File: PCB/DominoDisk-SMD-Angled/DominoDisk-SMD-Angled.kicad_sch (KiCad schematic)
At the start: 28 parts, among them J1 Daisy port out, J2 ICSP_ISP6, J3 UART, J4 Daisy port in, K1 HYC77-TF09-200, U1 PC817C-S, U2 ATmega328P-AU, U3 SE5218, U4 TXB0104QPWRQ1, Y1 Crystal_GND2

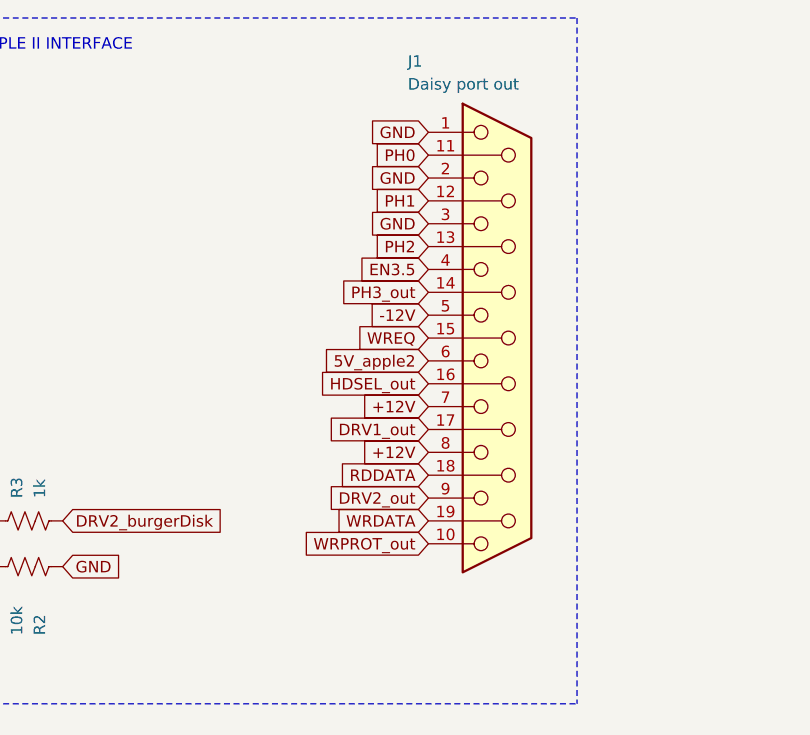
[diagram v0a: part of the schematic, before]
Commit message: Cleanup PCBs, fatter power traces
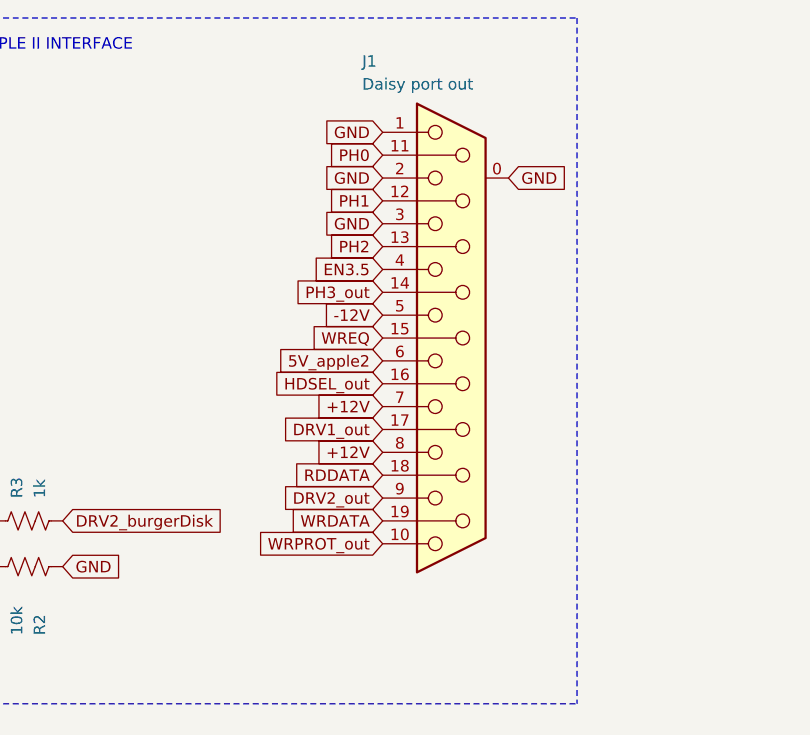
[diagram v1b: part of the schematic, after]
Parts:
- J1: footprint db19:DSUB-19_Female_EdgeMount_Pitch2.77mm -> DSUB-19-angled:DSUB-19_Female_Horizontal_MXS82009-8251-9246
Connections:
- net GND: now also J1.0 (GND)

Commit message: Add libraries and update Domino/Angled
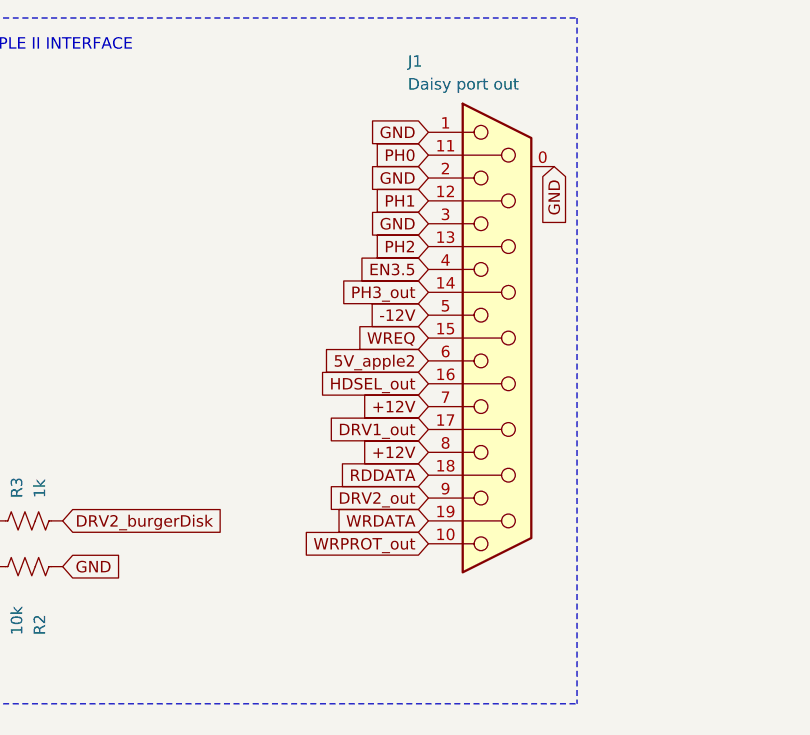
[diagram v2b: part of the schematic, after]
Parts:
- C2: value 100nF -> 100n; LCSC C28233 -> C1590
- K1: footprint MICROSD-HYC77-TF09-200:MICROSD-HYC77-TF09-200 -> HYC04-TF09-200:MICROSD-HYC77-TF09-200
- R4: value 10K -> 10k; LCSC C17414 -> C177337
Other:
- moved on the sheet: J1
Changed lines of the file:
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@@
 	(global_label "+12V"
 		(shape input)
-		(at 140.97 63.5 180)
+		(at 146.05 63.5 180)
 		(fields_autoplaced yes)
 		(effects
@@
 		)
 		(property "Intersheetrefs" "${INTERSHEET_REFS}"
-			(at 132.9048 63.5 0)
+			(at 137.9848 63.5 0)
 			(effects
 				(font
@@
 	(global_label "WRDATA"
 		(shape input)
-		(at 140.97 71.12 180)
+		(at 146.05 71.12 180)
 		(fields_autoplaced yes)
 		(effects
@@
 		)
 		(property "Intersheetrefs" "${INTERSHEET_REFS}"
-			(at 130.8486 71.12 0)
+			(at 135.9286 71.12 0)
 			(effects
 				(font
@@
 	(global_label "-12V"
 		(shape input)
-		(at 140.97 48.26 180)
+		(at 146.05 48.26 180)
 		(fields_autoplaced yes)
 		(effects
@@
 		)
 		(property "Intersheetrefs" "${INTERSHEET_REFS}"
-			(at 132.9048 48.26 0)
+			(at 137.9848 48.26 0)
 			(effects
 				(font
@@
 	(global_label "DRV2_out"
 		(shape input)
-		(at 140.97 68.58 180)
+		(at 146.05 68.58 180)
 		(fields_autoplaced yes)
 		(effects
@@
 		)
 		(property "Intersheetrefs" "${INTERSHEET_REFS}"
-			(at 129.1554 68.58 0)
+			(at 134.2354 68.58 0)
 			(effects
 				(font
@@
 	(global_label "GND"
 		(shape input)
-		(at 140.97 38.1 180)
+		(at 146.05 38.1 180)
 		(fields_autoplaced yes)
 		(effects
@@
 		)
 		(property "Intersheetrefs" "${INTERSHEET_REFS}"
-			(at 134.1143 38.1 0)
+			(at 139.1943 38.1 0)
 			(effects
 				(font
@@
 	(global_label "HDSEL_out"
 		(shape input)
-		(at 140.97 55.88 180)
+		(at 146.05 55.88 180)
 		(fields_autoplaced yes)
 		(effects
@@
 		)
 		(property "Intersheetrefs" "${INTERSHEET_REFS}"
-			(at 128.0064 55.88 0)
+			(at 133.0864 55.88 0)
+			(effects
+				(font
+					(size 1.27 1.27)
+				)
+				(justify right)
+				(hide yes)
+			)
+		)
+	)
+	(global_label "GND"
+		(shape input)
+		(at 160.02 31.75 270)
+		(fields_autoplaced yes)
+		(effects
+			(font
+				(size 1.27 1.27)
+			)
+			(justify right)
+		)
+		(property "Intersheetrefs" "${INTERSHEET_REFS}"
+			(at 160.02 38.6057 90)
 			(effects
 				(font
@@
 	(global_label "PH0"
 		(shape input)
-		(at 140.97 30.48 180)
+		(at 146.05 30.48 180)
 		(fields_autoplaced yes)
 		(effects
@@
 		)
 		(property "Intersheetrefs" "${INTERSHEET_REFS}"
-			(at 134.1748 30.48 0)
+			(at 139.2548 30.48 0)
 			(effects
 				(font
@@
 	(global_label "GND"
 		(shape input)
-		(at 154.94 33.02 0)
-		(fields_autoplaced yes)
-		(effects
-			(font
-				(size 1.27 1.27)
-			)
-			(justify left)
-		)
-		(property "Intersheetrefs" "${INTERSHEET_REFS}"
-			(at 161.7957 33.02 0)
-			(effects
-				(font
-					(size 1.27 1.27)
-				)
-				(justify left)
-				(hide yes)
-			)
-		)
-	)
-	(global_label "GND"
-		(shape input)
 		(at 41.91 27.94 0)
 		(fields_autoplaced yes)
@@
 	(global_label "RDDATA"
 		(shape input)
-		(at 140.97 66.04 180)
+		(at 146.05 66.04 180)
 		(fields_autoplaced yes)
 		(effects
@@
 		)
 		(property "Intersheetrefs" "${INTERSHEET_REFS}"
-			(at 131.03 66.04 0)
+			(at 136.11 66.04 0)
 			(effects
 				(font
@@
 	(global_label "GND"
 		(shape input)
-		(at 140.97 27.94 180)
+		(at 146.05 27.94 180)
 		(fields_autoplaced yes)
 		(effects
@@
 		)
 		(property "Intersheetrefs" "${INTERSHEET_REFS}"
-			(at 134.1143 27.94 0)
+			(at 139.1943 27.94 0)
 			(effects
 				(font
@@
 	(global_label "5V_apple2"
 		(shape input)
-		(at 140.97 53.34 180)
+		(at 146.05 53.34 180)
 		(fields_autoplaced yes)
 		(effects
@@
 		)
 		(property "Intersheetrefs" "${INTERSHEET_REFS}"
-			(at 128.3088 53.34 0)
+			(at 133.3888 53.34 0)
 			(effects
 				(font
@@
 	(global_label "GND"
 		(shape input)
-		(at 140.97 33.02 180)
+		(at 146.05 33.02 180)
 		(fields_autoplaced yes)
 		(effects
@@
 		)
 		(property "Intersheetrefs" "${INTERSHEET_REFS}"
-			(at 134.1143 33.02 0)
+			(at 139.1943 33.02 0)
 			(effects
 				(font
@@
 	(global_label "WREQ"
 		(shape input)
-		(at 140.97 50.8 180)
+		(at 146.05 50.8 180)
 		(fields_autoplaced yes)
 		(effects
@@
 		)
 		(property "Intersheetrefs" "${INTERSHEET_REFS}"
-			(at 132.7839 50.8 0)
+			(at 137.8639 50.8 0)
 			(effects
 				(font
@@
 	(global_label "DRV1_out"
 		(shape input)
-		(at 140.97 60.96 180)
+		(at 146.05 60.96 180)
 		(fields_autoplaced yes)
 		(effects
@@
 		)
 		(property "Intersheetrefs" "${INTERSHEET_REFS}"
-			(at 129.1554 60.96 0)
+			(at 134.2354 60.96 0)
 			(effects
 				(font
@@
 	(global_label "PH2"
 		(shape input)
-		(at 140.97 40.64 180)
+		(at 146.05 40.64 180)
 		(fields_autoplaced yes)
 		(effects
@@
 		)
 		(property "Intersheetrefs" "${INTERSHEET_REFS}"
-			(at 134.1748 40.64 0)
+			(at 139.2548 40.64 0)
 			(effects
 				(font
@@
 	(global_label "PH1"
 		(shape input)
-		(at 140.97 35.56 180)
+		(at 146.05 35.56 180)
 		(fields_autoplaced yes)
 		(effects
@@
 		)
 		(property "Intersheetrefs" "${INTERSHEET_REFS}"
-			(at 134.1748 35.56 0)
+			(at 139.2548 35.56 0)
 			(effects
 				(font
@@
 	(global_label "EN3.5"
 		(shape input)
-		(at 140.97 43.18 180)
+		(at 146.05 43.18 180)
 		(fields_autoplaced yes)
 		(effects
@@
 		)
 		(property "Intersheetrefs" "${INTERSHEET_REFS}"
-			(at 132.4815 43.18 0)
+			(at 137.5615 43.18 0)
 			(effects
 				(font
@@
 	(global_label "PH3_out"
 		(shape input)
-		(at 140.97 45.72 180)
+		(at 146.05 45.72 180)
 		(fields_autoplaced yes)
 		(effects
@@
 		)
 		(property "Intersheetrefs" "${INTERSHEET_REFS}"
-			(at 130.1835 45.72 0)
+			(at 135.2635 45.72 0)
 			(effects
 				(font
@@
 	(global_label "+12V"
 		(shape input)
-		(at 140.97 58.42 180)
+		(at 146.05 58.42 180)
 		(fields_autoplaced yes)
 		(effects
@@
 		)
 		(property "Intersheetrefs" "${INTERSHEET_REFS}"
-			(at 132.9048 58.42 0)
+			(at 137.9848 58.42 0)
 			(effects
 				(font
@@
 	(global_label "WRPROT_out"
 		(shape input)
-		(at 140.97 73.66 180)
+		(at 146.05 73.66 180)
 		(fields_autoplaced yes)
 		(effects
@@
 		)
 		(property "Intersheetrefs" "${INTERSHEET_REFS}"
-			(at 126.434 73.66 0)
+			(at 131.514 73.66 0)
 			(effects
 				(font
@@
 			)
 		)
-		(property "Value" "100nF"
+		(property "Value" "100n"
 			(at 25.7048 118.11 90)
 			(effects
@@
 			)
 		)
-		(property "LCSC" "C28233"
+		(property "LCSC" " C1590"
 			(at 29.21 118.11 90)
 			(effects
@@
 	(symbol
 		(lib_id "db19:DB19_Female")
-		(at 148.59 50.8 0)
+		(at 153.67 50.8 0)
 		(unit 1)
 		(exclude_from_sim no)
@@
 		(dnp no)
 		(property "Reference" "J1"
-			(at 138.684 20.066 0)
+			(at 143.764 20.066 0)
 			(effects
 				(font
@@
 		)
 		(property "Value" "Daisy port out"
-			(at 138.684 22.606 0)
+			(at 143.764 22.606 0)
 			(effects
 				(font
@@
 		)
 		(property "Footprint" "DSUB-19-angled:DSUB-19_Female_Horizontal_MXS82009-8251-9246"
-			(at 148.59 58.42 0)
+			(at 153.67 58.42 0)
 			(effects
 				(font
@@
 		)
 		(property "Datasheet" ""
-			(at 148.59 58.42 0)
+			(at 153.67 58.42 0)
 			(effects
 				(font
@@
 		)
 		(property "Description" ""
-			(at 148.59 50.8 0)
+			(at 153.67 50.8 0)
 			(effects
 				(font
@@
 			)
 		)
-		(property "Footprint" "MICROSD-HYC77-TF09-200:MICROSD-HYC77-TF09-200"
+		(property "Footprint" "HYC04-TF09-200:MICROSD-HYC77-TF09-200"
 			(at 269.24 50.8 0)
 			(effects
@@
 			)
 		)
-		(property "Value" "10K"
+		(property "Value" "10k"
 			(at 108.4072 147.193 0)
 			(effects
@@
 			)
 		)
-		(property "LCSC" "C17414"
+		(property "LCSC" " C177337"
 			(at 106.68 146.05 0)
 			(effects

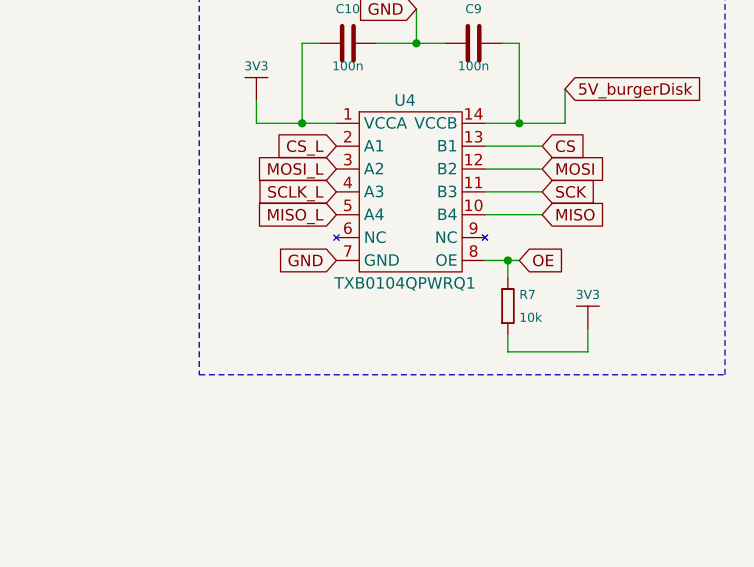
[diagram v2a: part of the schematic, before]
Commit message: Add logo (thanks to Javier Rivera!!)
Add my own micro/SD modules
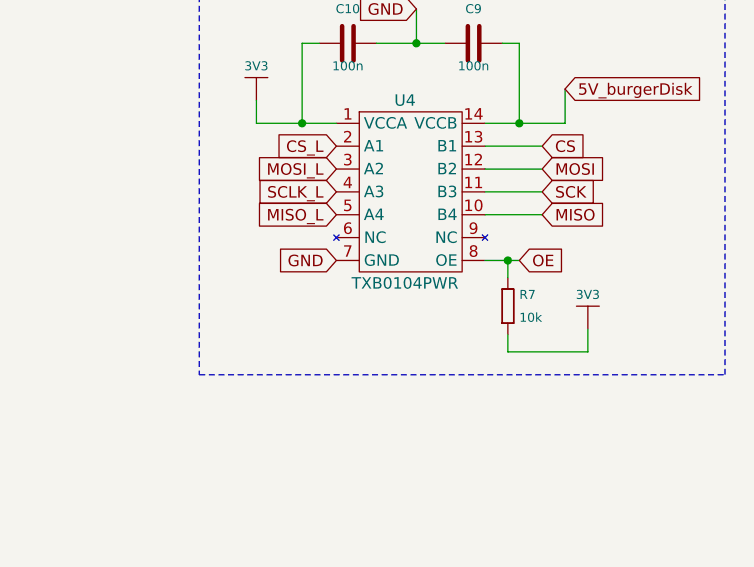
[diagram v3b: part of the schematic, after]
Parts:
- U4: value TXB0104QPWRQ1 -> TXB0104PWR; LCSC C527571 -> C60708
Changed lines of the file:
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@@
 			)
 		)
-		(property "Value" "TXB0104QPWRQ1"
+		(property "Value" "TXB0104PWR"
 			(at 245.11 149.86 0)
 			(effects
@@
 			)
 		)
-		(property "LCSC" "C527571"
+		(property "LCSC" "C60708"
 			(at 245.11 138.43 0)
 			(effects

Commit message: Update from -SMD
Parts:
- D3: LCSC C2288 -> C965807
- R6: value 150 -> 100; LCSC C177290 -> C22369795
- Y1: value Crystal_GND2 -> Resonator
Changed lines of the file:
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@@
 		)
 	)
-	(global_label "GND"
-		(shape input)
-		(at 160.02 31.75 270)
-		(fields_autoplaced yes)
-		(effects
-			(font
-				(size 1.27 1.27)
-			)
-			(justify right)
-		)
-		(property "Intersheetrefs" "${INTERSHEET_REFS}"
-			(at 160.02 38.6057 90)
-			(effects
-				(font
-					(size 1.27 1.27)
-				)
-				(justify right)
-				(hide yes)
-			)
-		)
-	)
 	(global_label "LED"
 		(shape input)
@@
 		)
 	)
+	(global_label "GND"
+		(shape input)
+		(at 160.02 34.29 270)
+		(fields_autoplaced yes)
+		(effects
+			(font
+				(size 1.27 1.27)
+			)
+			(justify right)
+		)
+		(property "Intersheetrefs" "${INTERSHEET_REFS}"
+			(at 160.02 41.1457 90)
+			(effects
+				(font
+					(size 1.27 1.27)
+				)
+				(justify right)
+				(hide yes)
+			)
+		)
+	)
 	(global_label "SCLK_L"
 		(shape input)
@@
 		(on_board yes)
 		(dnp no)
-		(fields_autoplaced yes)
 		(property "Reference" "D3"
 			(at 122.2375 154.94 90)
@@
 			)
 		)
-		(property "Description" ""
-			(at 121.92 158.75 0)
+		(property "Description" "Blue LED, 20mA 3.3V"
+			(at 121.666 162.814 0)
 			(effects
 				(font
@@
 			)
 		)
-		(property "LCSC" "C2288"
+		(property "LCSC" "C965807"
 			(at 121.92 158.75 0)
 			(effects
@@
 			)
 		)
-		(property "Value" "150"
+		(property "Value" "100"
 			(at 115.57 156.21 0)
 			(effects
@@
 			)
 		)
-		(property "LCSC" "C177290"
+		(property "LCSC" "C22369795"
 			(at 114.3 158.75 0)
 			(effects
@@
 			)
 		)
-		(property "Value" "Crystal_GND2"
+		(property "Value" "Resonator"
 			(at 99.06 128.27 0)
 			(effects
@@
 			)
 		)
-		(property "Description" "Three pin crystal, GND on pin 2"
+		(property "Description" "Three pin, GND on pin 2"
 			(at 99.06 133.35 0)
 			(effects

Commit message: Update details
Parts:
- removed C5: 2u2, Capacitor_SMD:C_0603_1608Metric, symbol e-radionica.com schematics:0603C
- removed C6: 100n, Capacitor_SMD:C_0603_1608Metric, symbol e-radionica.com schematics:0603C
- C1: renamed from C7; value 100n -> 22uF; footprint Capacitor_SMD:C_0603_1608Metric -> Capacitor_SMD:C_0805_2012Metric; LCSC C1590 -> C45783
- C2: renamed from C9; LCSC C1590 -> C14663
- C3: renamed from C10; LCSC C1590 -> C14663
- C4: renamed from C2; LCSC C1590 -> C14663
- J4: renamed from J3; footprint Connector_PinHeader_2.54mm:PinHeader_1x02_P2.54mm_Horizontal -> Connector_PinHeader_2.54mm:PinHeader_1x02_P2.54mm_Vertical
- K1: value HYC77-TF09-200 -> TF-104 MicroSD card holder; footprint HYC04-TF09-200:MICROSD-HYC77-TF09-200 -> TF-104:TF-SMD_TF-104; LCSC C341092 -> C266612
- R1: renamed from R6; LCSC C22369795 -> C22775
- R3: renamed from R4; LCSC C177337 -> C25804
- R4: renamed from R7; LCSC C177337 -> C25804
- R5: renamed from R3; LCSC C177343 -> C21190
- R6: renamed from R2; LCSC C177337 -> C25804
- R7: renamed from R5; LCSC C177341 -> C23138
- U3: renamed from U4; value TXB0104PWR -> TXB0104PWR level shifter
- U4: renamed from U3; value SE5218 -> SE5218ALG voltage regulator
- Y1: value Resonator -> CSTNE16M0V530000R0 Resonator
- renumbered C8 to C5, C4 to C6, D3 to D1, D1 to D2, D2 to D3, J4 to J3, R1 to R2
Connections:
- net GND: now also K1.10, K1.9

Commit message: Move to bigger pads for diodes
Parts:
- D3: footprint Diode_SMD:D_SOD-323F -> Diode_SMD:D_SOD-323_HandSoldering
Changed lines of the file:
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@@
 			)
 		)
-		(property "Footprint" "Diode_SMD:D_SOD-323F"
+		(property "Footprint" "Diode_SMD:D_SOD-323_HandSoldering"
 			(at 54.61 69.215 0)
 			(effects
